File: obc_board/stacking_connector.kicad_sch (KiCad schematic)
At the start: 49 parts, among them U27 AP22652A, U5 LTC4304IMS#PBF, U6 PC104, U7 LTC4304IMS#PBF

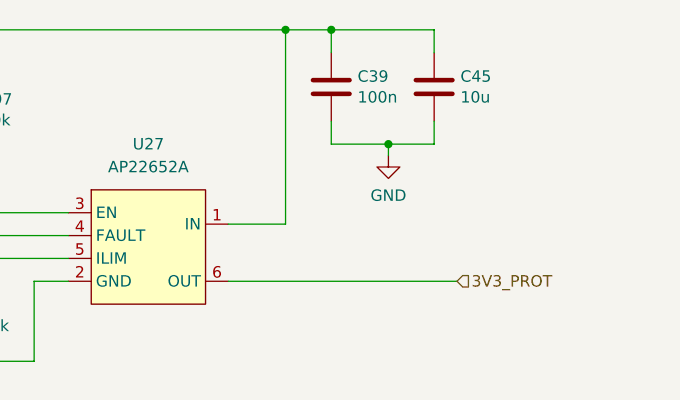
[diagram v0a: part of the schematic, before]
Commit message: routed photodiode circuits, jtag and short circuit prot circuits
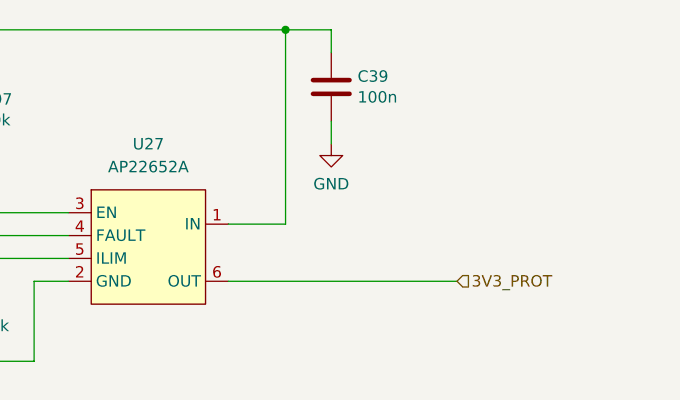
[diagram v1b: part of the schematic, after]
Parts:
- removed C45: 10u, Capacitor_SMD:C_1206_3216Metric, symbol Device:C
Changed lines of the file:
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@@
   (junction (at 144.78 119.38) (diameter 0) (color 0 0 0 0)
   )
-  (junction (at 238.76 20.32) (diameter 0) (color 0 0 0 0)
-  )
   (junction (at 43.18 85.09) (diameter 0) (color 0 0 0 0)
   )
@@
   )
   (junction (at 205.74 106.68) (diameter 0) (color 0 0 0 0)
-  )
-  (junction (at 245.11 33.02) (diameter 0) (color 0 0 0 0)
   )
   (junction (at 198.12 20.32) (diameter 0) (color 0 0 0 0)
@@
     (stroke (width 0) (type default) (color 0 0 0 0))
   )
-  (wire (pts (xy 250.19 33.02) (xy 245.11 33.02))
-    (stroke (width 0) (type default) (color 0 0 0 0))
-  )
   (wire (pts (xy 205.74 48.26) (xy 209.55 48.26))
     (stroke (width 0) (type default) (color 0 0 0 0))
@@
     (stroke (width 0) (type default) (color 0 0 0 0))
   )
-  (wire (pts (xy 245.11 33.02) (xy 245.11 34.29))
-    (stroke (width 0) (type default) (color 0 0 0 0))
-  )
   (wire (pts (xy 199.39 71.12) (xy 199.39 76.2))
     (stroke (width 0) (type default) (color 0 0 0 0))
@@
     (stroke (width 0) (type default) (color 0 0 0 0))
   )
-  (wire (pts (xy 250.19 22.86) (xy 250.19 20.32))
-    (stroke (width 0) (type default) (color 0 0 0 0))
-  )
   (wire (pts (xy 144.78 143.51) (xy 152.4 143.51))
     (stroke (width 0) (type default) (color 0 0 0 0))
@@
     (stroke (width 0) (type default) (color 0 0 0 0))
   )
-  (wire (pts (xy 245.11 33.02) (xy 238.76 33.02))
-    (stroke (width 0) (type default) (color 0 0 0 0))
-  )
   (wire (pts (xy 209.55 45.72) (xy 196.85 45.72))
     (stroke (width 0) (type default) (color 0 0 0 0))
@@
     (stroke (width 0) (type default) (color 0 0 0 0))
   )
-  (wire (pts (xy 250.19 20.32) (xy 238.76 20.32))
-    (stroke (width 0) (type default) (color 0 0 0 0))
-  )
   (wire (pts (xy 269.24 106.68) (xy 269.24 111.76))
     (stroke (width 0) (type default) (color 0 0 0 0))
@@
   )
   (wire (pts (xy 27.94 146.05) (xy 27.94 147.32))
-    (stroke (width 0) (type default) (color 0 0 0 0))
-  )
-  (wire (pts (xy 250.19 30.48) (xy 250.19 33.02))
     (stroke (width 0) (type default) (color 0 0 0 0))
   )
@@
     (pin "2")
   )
-  (symbol (lib_id "power:GND") (at 245.11 34.29 0) (unit 1)
+  (symbol (lib_id "power:GND") (at 238.76 33.02 0) (unit 1)
     (in_bom yes) (on_board yes) (fields_autoplaced)
-    (property "Reference" "#PWR0107" (id 0) (at 245.11 40.64 0)
-      (effects (font (size 1.27 1.27)) hide)
-    )
-    (property "Value" "GND" (id 1) (at 245.11 38.7334 0))
-    (property "Footprint" "" (id 2) (at 245.11 34.29 0)
-      (effects (font (size 1.27 1.27)) hide)
-    )
-    (property "Datasheet" "" (id 3) (at 245.11 34.29 0)
+    (property "Reference" "#PWR0107" (id 0) (at 238.76 39.37 0)
+      (effects (font (size 1.27 1.27)) hide)
+    )
+    (property "Value" "GND" (id 1) (at 238.76 37.4634 0))
+    (property "Footprint" "" (id 2) (at 238.76 33.02 0)
+      (effects (font (size 1.27 1.27)) hide)
+    )
+    (property "Datasheet" "" (id 3) (at 238.76 33.02 0)
       (effects (font (size 1.27 1.27)) hide)
     )
@@
     (pin "1")
   )
-  (symbol (lib_id "Device:C") (at 250.19 26.67 0) (unit 1)
-    (in_bom yes) (on_board yes)
-    (property "Reference" "C45" (id 0) (at 253.111 25.5016 0)
-      (effects (font (size 1.27 1.27)) (justify left))
-    )
-    (property "Value" "10u" (id 1) (at 253.111 27.813 0)
-      (effects (font (size 1.27 1.27)) (justify left))
-    )
-    (property "Footprint" "Capacitor_SMD:C_1206_3216Metric" (id 2) (at 251.1552 30.48 0)
-      (effects (font (size 1.27 1.27)) hide)
-    )
-    (property "Datasheet" "~" (id 3) (at 250.19 26.67 0)
-      (effects (font (size 1.27 1.27)) hide)
-    )
-    (property "Digikey Part Number" "399-7012-1-ND" (id 4) (at 250.19 26.67 0)
-      (effects (font (size 1.27 1.27)) hide)
-    )
-    (pin "1")
-    (pin "2")
-  )
   (symbol (lib_id "Connector:TestPoint") (at 217.17 151.13 0) (unit 1)
